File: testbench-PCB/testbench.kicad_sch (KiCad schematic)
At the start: 1 part, among them U5 ATmega328P_Xplained_Mini

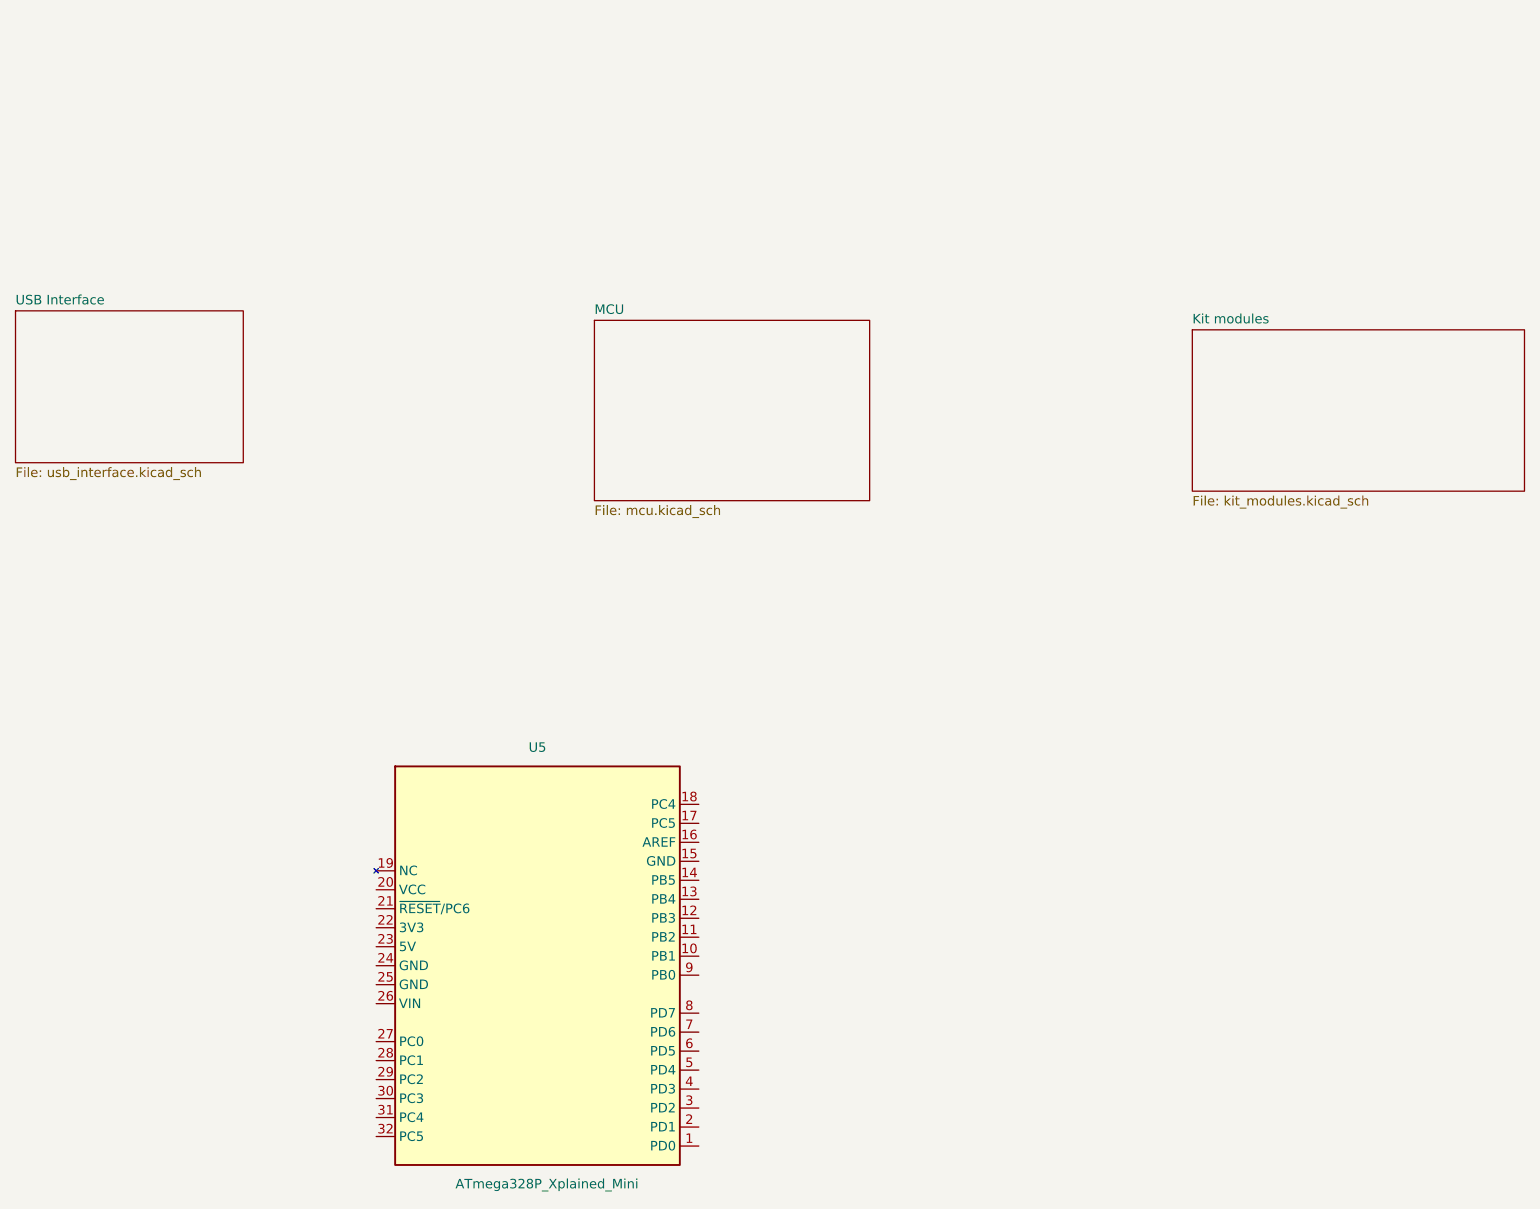
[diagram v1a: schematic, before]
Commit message: Added connection between some modules.
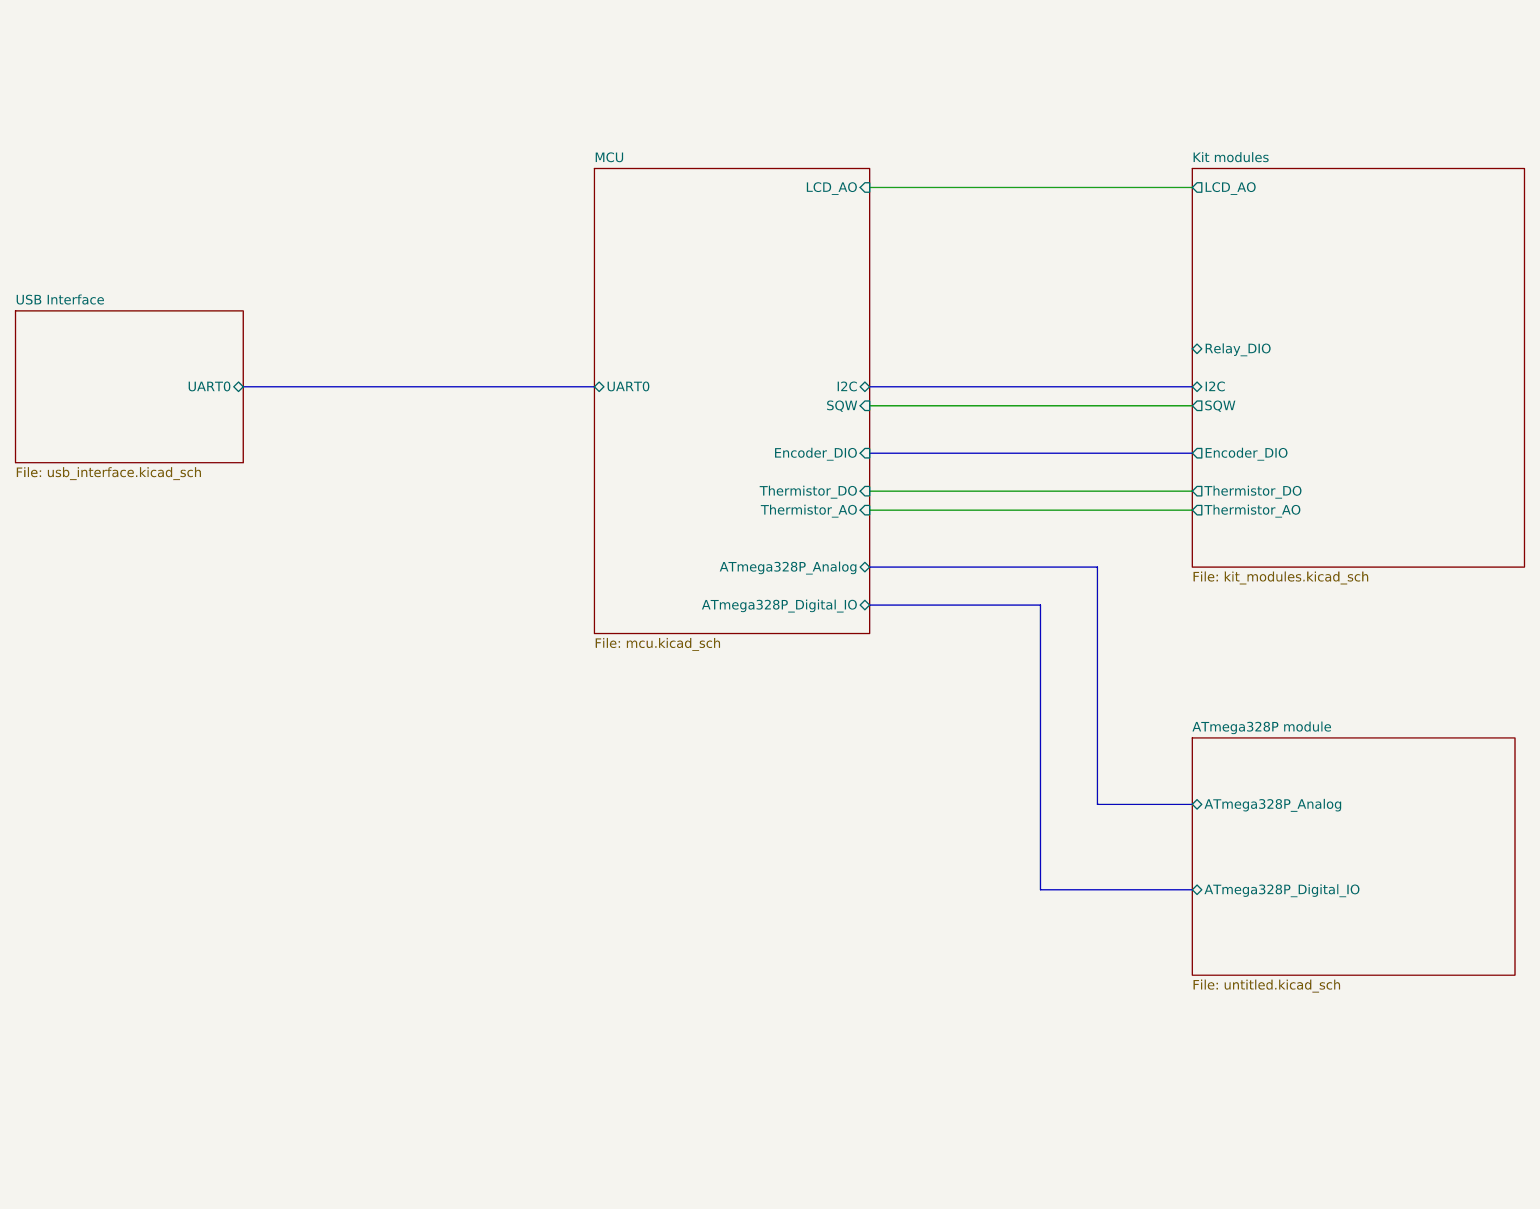
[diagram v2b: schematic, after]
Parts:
- removed U5: ATmega328P_Xplained_Mini, kit_modules:ATmega328P_Xplained_Mini, symbol kit_modules:ATmega328P_Xplained_mini
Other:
- added sheet ATmega328P module (untitled.kicad_sch)
- sheet Kit modules ports: added Encoder_DIO, I2C, LCD_AO, Relay_DIO, SQW, Thermistor_AO, Thermistor_DO; removed none
- sheet MCU ports: added ATmega328P_Analog, ATmega328P_Digital_IO, Encoder_DIO, I2C, LCD_AO, SQW, Thermistor_AO, Thermistor_DO, UART0; removed none
- sheet USB Interface ports: added UART0; removed none
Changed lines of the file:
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@@
 (kicad_sch (version 20230121) (generator eeschema)
   (paper "A4")
-  (symbol (lib_id "kit_modules:ATmega328P_Xplained_mini") (at 95.25 113.03 0) (unit 1)
-    (in_bom yes) (on_board yes) (dnp no)
-    (property "Reference" "U5" (at 104.14 119.38 0)
-      (effects (font (size 1.27 1.27)))
-    )
-    (property "Value" "ATmega328P_Xplained_Mini" (at 105.41 177.8 0)
-      (effects (font (size 1.27 1.27)))
-    )
-    (property "Footprint" "kit_modules:ATmega328P_Xplained_Mini" (at 88.9 121.92 0)
-      (effects (font (size 1.27 1.27)) hide)
-    )
-    (property "Datasheet" "" (at 88.9 121.92 0)
-      (effects (font (size 1.27 1.27)) hide)
-    )
-    (pin "1")
-    (pin "10")
-    (pin "11")
-    (pin "12")
-    (pin "13")
-    (pin "14")
-    (pin "15")
-    (pin "16")
-    (pin "17")
-    (pin "18")
-    (pin "19")
-    (pin "2")
-    (pin "20")
-    (pin "21")
-    (pin "22")
-    (pin "23")
-    (pin "24")
-    (pin "25")
-    (pin "26")
-    (pin "27")
-    (pin "28")
-    (pin "29")
-    (pin "3")
-    (pin "30")
-    (pin "31")
-    (pin "32")
-    (pin "4")
-    (pin "5")
-    (pin "6")
-    (pin "7")
-    (pin "8")
-    (pin "9")
-    (instances
-      (project "testbench"
-        (path "/3ac6901d-218d-4b34-8c4a-bf7c417c33bc"
-          (reference "U5") (unit 1)
-        )
-      )
-    )
+  (bus (pts (xy 148.59 80.01) (xy 191.77 80.01))
+    (stroke (width 0) (type default))
   )
-  (sheet (at 111.76 62.23) (size 36.83 24.13) (fields_autoplaced)
+  (bus (pts (xy 64.77 71.12) (xy 111.76 71.12))
+    (stroke (width 0) (type default))
+  )
+  (bus (pts (xy 171.45 138.43) (xy 191.77 138.43))
+    (stroke (width 0) (type default))
+  )
+  (wire (pts (xy 148.59 73.66) (xy 191.77 73.66))
+    (stroke (width 0) (type default))
+  )
+  (bus (pts (xy 171.45 100.33) (xy 171.45 138.43))
+    (stroke (width 0) (type default))
+  )
+  (bus (pts (xy 148.59 95.25) (xy 179.07 95.25))
+    (stroke (width 0) (type default))
+  )
+  (wire (pts (xy 148.59 85.09) (xy 191.77 85.09))
+    (stroke (width 0) (type default))
+  )
+  (bus (pts (xy 179.07 95.25) (xy 179.07 127))
+    (stroke (width 0) (type default))
+  )
+  (wire (pts (xy 148.59 87.63) (xy 191.77 87.63))
+    (stroke (width 0) (type default))
+  )
+  (wire (pts (xy 148.59 44.45) (xy 191.77 44.45))
+    (stroke (width 0) (type default))
+  )
+  (bus (pts (xy 179.07 127) (xy 191.77 127))
+    (stroke (width 0) (type default))
+  )
+  (bus (pts (xy 148.59 71.12) (xy 191.77 71.12))
+    (stroke (width 0) (type default))
+  )
+  (bus (pts (xy 148.59 100.33) (xy 171.45 100.33))
+    (stroke (width 0) (type default))
+  )
+  (sheet (at 111.76 41.91) (size 36.83 62.23) (fields_autoplaced)
     (stroke (width 0.1524) (type solid))
     (fill (color 255 229 191 1.0000))
-    (property "Sheetname" "MCU" (at 111.76 61.5184 0)
+    (property "Sheetname" "MCU" (at 111.76 41.1984 0)
       (effects (font (size 1.27 1.27)) (justify left bottom))
     )
-    (property "Sheetfile" "mcu.kicad_sch" (at 111.76 86.9446 0)
+    (property "Sheetfile" "mcu.kicad_sch" (at 111.76 104.7246 0)
       (effects (font (size 1.27 1.27)) (justify left top))
+    )
+    (pin "UART0" bidirectional (at 111.76 71.12 180)
+      (effects (font (size 1.27 1.27)) (justify left))
+    )
+    (pin "I2C" bidirectional (at 148.59 71.12 0)
+      (effects (font (size 1.27 1.27)) (justify right))
+    )
+    (pin "SQW" input (at 148.59 73.66 0)
+      (effects (font (size 1.27 1.27)) (justify right))
+    )
+    (pin "ATmega328P_Analog" bidirectional (at 148.59 95.25 0)
+      (effects (font (size 1.27 1.27)) (justify right))
+    )
+    (pin "ATmega328P_Digital_IO" bidirectional (at 148.59 100.33 0)
+      (effects (font (size 1.27 1.27)) (justify right))
+    )
+    (pin "Encoder_DIO" input (at 148.59 80.01 0)
+      (effects (font (size 1.27 1.27)) (justify right))
+    )
+    (pin "LCD_AO" input (at 148.59 44.45 0)
+      (effects (font (size 1.27 1.27)) (justify right))
+    )
+    (pin "Thermistor_AO" input (at 148.59 87.63 0)
+      (effects (font (size 1.27 1.27)) (justify right))
+    )
+    (pin "Thermistor_DO" input (at 148.59 85.09 0)
+      (effects (font (size 1.27 1.27)) (justify right))
     )
     (instances
@@
     )
   )
-  (sheet (at 191.77 63.5) (size 44.45 21.59) (fields_autoplaced)
+  (sheet (at 191.77 118.11) (size 43.18 31.75) (fields_autoplaced)
     (stroke (width 0.1524) (type solid))
     (fill (color 255 229 191 1.0000))
-    (property "Sheetname" "Kit modules" (at 191.77 62.7884 0)
+    (property "Sheetname" "ATmega328P module" (at 191.77 117.3984 0)
       (effects (font (size 1.27 1.27)) (justify left bottom))
     )
-    (property "Sheetfile" "kit_modules.kicad_sch" (at 191.77 85.6746 0)
+    (property "Sheetfile" "untitled.kicad_sch" (at 191.77 150.4446 0)
       (effects (font (size 1.27 1.27)) (justify left top))
+    )
+    (pin "ATmega328P_Analog" bidirectional (at 191.77 127 180)
+      (effects (font (size 1.27 1.27)) (justify left))
+    )
+    (pin "ATmega328P_Digital_IO" bidirectional (at 191.77 138.43 180)
+      (effects (font (size 1.27 1.27)) (justify left))
+    )
+    (instances
+      (project "testbench"
+        (path "/3ac6901d-218d-4b34-8c4a-bf7c417c33bc" (page "5"))
+      )
+    )
+  )
+  (sheet (at 191.77 41.91) (size 44.45 53.34) (fields_autoplaced)
+    (stroke (width 0.1524) (type solid))
+    (fill (color 255 229 191 1.0000))
+    (property "Sheetname" "Kit modules" (at 191.77 41.1984 0)
+      (effects (font (size 1.27 1.27)) (justify left bottom))
+    )
+    (property "Sheetfile" "kit_modules.kicad_sch" (at 191.77 95.8346 0)
+      (effects (font (size 1.27 1.27)) (justify left top))
+    )
+    (pin "Relay_DIO" bidirectional (at 191.77 66.04 180)
+      (effects (font (size 1.27 1.27)) (justify left))
+    )
+    (pin "I2C" bidirectional (at 191.77 71.12 180)
+      (effects (font (size 1.27 1.27)) (justify left))
+    )
+    (pin "SQW" output (at 191.77 73.66 180)
+      (effects (font (size 1.27 1.27)) (justify left))
+    )
+    (pin "Encoder_DIO" output (at 191.77 80.01 180)
+      (effects (font (size 1.27 1.27)) (justify left))
+    )
+    (pin "Thermistor_DO" output (at 191.77 85.09 180)
+      (effects (font (size 1.27 1.27)) (justify left))
+    )
+    (pin "Thermistor_AO" output (at 191.77 87.63 180)
+      (effects (font (size 1.27 1.27)) (justify left))
+    )
+    (pin "LCD_AO" output (at 191.77 44.45 180)
+      (effects (font (size 1.27 1.27)) (justify left))
     )
     (instances
@@
       (effects (font (size 1.27 1.27)) (justify left top))
     )
+    (pin "UART0" bidirectional (at 64.77 71.12 0)
+      (effects (font (size 1.27 1.27)) (justify right))
+    )
     (instances
